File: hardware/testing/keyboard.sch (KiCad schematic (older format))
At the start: 1 part

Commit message: starting the testing PCB
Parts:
- removed U_Main1: proton_c, proton_c:proton_c, symbol proton_c:proton_c
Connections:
- no-connect marks 37 -> 0
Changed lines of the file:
@@
 $Descr A4 11693 8268
 encoding utf-8
-Sheet 1 2
+Sheet 1 5
 Title ""
 Date ""
@@
 $EndDescr
 $Sheet
-S 1650 2250 1900 1550
+S 3750 2750 700  1950
 U 5E25E984
 F0 "switch" 50
 F1 "switch.sch" 50
-F2 "ROW1" I R 3550 2300 50
-F3 "ROW2" I R 3550 2400 50
-F4 "ROW3" I R 3550 2500 50
-F5 "ROW4" I R 3550 2600 50
-F6 "COL1" I L 1650 2300 50
-F7 "COL2" I L 1650 2400 50
-F8 "COL3" I L 1650 2500 50
-F9 "COL4" I L 1650 2600 50
+F2 "ROW1" I R 4450 4600 50
+F3 "ROW2" I R 4450 4500 50
+F4 "ROW3" I R 4450 4400 50
+F5 "ROW4" I R 4450 4300 50
+F6 "ROW5" I R 4450 4200 50
+F7 "COL1" I R 4450 2800 50
+F8 "COL2" I R 4450 2900 50
+F9 "COL3" I R 4450 3000 50
+F10 "COL4" I R 4450 3100 50
+F11 "COL5" I R 4450 3200 50
+F12 "COL6" I R 4450 3300 50
+F13 "COL7" I R 4450 3400 50
+F14 "COL8" I R 4450 3500 50
+F15 "COL9" I R 4450 3600 50
+F16 "COL10" I R 4450 3700 50
+F17 "COL11" I R 4450 3800 50
+F18 "COL12" I R 4450 3900 50
+F19 "COL13" I R 4450 4000 50
+F20 "COL14" I R 4450 4100 50
+$EndSheet
+$Sheet
+S 5500 2450 800  2250
+U 5E1424B2
+F0 "SMT32" 50
+F1 "SMT32.sch" 50
+F2 "I2C2_SDA" I R 6300 2900 50
+F3 "I2C2_SCL" I R 6300 2800 50
+F4 "COL1" I L 5500 2800 50
+F5 "COL2" I L 5500 2900 50
+F6 "COL3" I L 5500 3000 50
+F7 "COL4" I L 5500 3100 50
+F8 "COL5" I L 5500 3200 50
+F9 "COL6" I L 5500 3300 50
+F10 "COL7" I L 5500 3400 50
+F11 "COL8" I L 5500 3500 50
+F12 "COL9" I L 5500 3600 50
+F13 "COL10" I L 5500 3700 50
+F14 "COL11" I L 5500 3800 50
+F15 "COL12" I L 5500 3900 50
+F16 "COL13" I L 5500 4000 50
+F17 "COL14" I L 5500 4100 50
+F18 "ROW5" I L 5500 4200 50
+F19 "ROW4" I L 5500 4300 50
+F20 "ROW3" I L 5500 4400 50
+F21 "ROW2" I L 5500 4500 50
+F22 "ROW1" I L 5500 4600 50
+F23 "LED_EN_PIN" I R 6300 3000 50
 $EndSheet
 Wire Wire Line
-	7050 2350 3600 2350
+	5500 2800 4450 2800
 Wire Wire Line
-	3600 2350 3600 2400
+	4450 2900 5500 2900
 Wire Wire Line
-	3600 2400 3550 2400
+	5500 3000 4450 3000
 Wire Wire Line
-	7050 2450 3600 2450
+	4450 3100 5500 3100
 Wire Wire Line
-	3600 2450 3600 2500
+	5500 3200 4450 3200
 Wire Wire Line
-	3600 2500 3550 2500
+	4450 3300 5500 3300
 Wire Wire Line
-	3550 2600 3600 2600
+	5500 3400 4450 3400
 Wire Wire Line
-	3600 2600 3600 2550
+	4450 3500 5500 3500
 Wire Wire Line
-	3600 2550 7050 2550
+	5500 3600 4450 3600
 Wire Wire Line
-	7050 2050 3600 2050
+	4450 3700 5500 3700
 Wire Wire Line
-	3600 2050 3600 2300
+	5500 3800 4450 3800
 Wire Wire Line
-	3600 2300 3550 2300
+	4450 3900 5500 3900
 Wire Wire Line
-	1650 2300 1550 2300
+	5500 4000 4450 4000
 Wire Wire Line
-	1550 2300 1550 1500
+	4450 4100 5500 4100
 Wire Wire Line
-	1550 1500 9200 1500
+	5500 4200 4450 4200
 Wire Wire Line
-	9200 1500 9200 2350
+	4450 4300 5500 4300
 Wire Wire Line
-	9200 2350 9100 2350
+	5500 4400 4450 4400
 Wire Wire Line
-	9100 2450 9250 2450
+	4450 4500 5500 4500
 Wire Wire Line
-	9250 2450 9250 1400
+	5500 4600 4450 4600
 Wire Wire Line
-	9250 1400 1500 1400
+	6300 3000 6700 3000
 Wire Wire Line
-	1500 1400 1500 2400
+	6700 2900 6300 2900
 Wire Wire Line
-	1500 2400 1650 2400
-Wire Wire Line
-	1650 2500 1450 2500
-Wire Wire Line
-	1450 2500 1450 1300
-Wire Wire Line
-	9300 1300 9300 2550
-Wire Wire Line
-	9300 2550 9100 2550
-Wire Wire Line
-	1400 1250 9350 1250
-Wire Wire Line
-	9350 1250 9350 2650
-Wire Wire Line
-	9350 2650 9100 2650
-Wire Wire Line
-	1450 1300 9300 1300
-$Comp
-L proton_c:proton_c U_Main1
-U 1 1 5E06F676
-P 8100 2950
-F 0 "U_Main1" H 8075 1427 50  0000 C CNN
-F 1 "proton_c" H 8075 1336 50  0000 C CNN
-F 2 "proton_c:proton_c" H 7950 2950 50  0001 C CNN
-F 3 "" H 7950 2950 50  0001 C CNN
-	1    8100 2950
-	1    0    0    -1
-$EndComp
-Wire Wire Line
-	1400 1250 1400 2600
-Wire Wire Line
-	1400 2600 1650 2600
-NoConn ~ 9100 1950
-NoConn ~ 9100 2050
-NoConn ~ 9100 2150
-NoConn ~ 9100 2250
-NoConn ~ 9100 2750
-NoConn ~ 9100 2850
-NoConn ~ 9100 2950
-NoConn ~ 8250 1650
-NoConn ~ 7900 1650
-NoConn ~ 7800 1650
-NoConn ~ 7700 1650
-NoConn ~ 7050 1950
-NoConn ~ 7050 2150
-NoConn ~ 7050 2250
-NoConn ~ 7050 2650
-NoConn ~ 7050 2750
-NoConn ~ 7050 2850
-NoConn ~ 7050 2950
-NoConn ~ 7050 3050
-NoConn ~ 7050 3400
-NoConn ~ 7050 3850
-NoConn ~ 7050 3950
-NoConn ~ 7050 4050
-NoConn ~ 7050 4150
-NoConn ~ 7050 4250
-NoConn ~ 7050 4350
-NoConn ~ 9100 4350
-NoConn ~ 9100 4250
-NoConn ~ 9100 4150
-NoConn ~ 9100 4050
-NoConn ~ 9100 3950
-NoConn ~ 9100 3850
-NoConn ~ 9100 3550
-NoConn ~ 9100 3450
-NoConn ~ 9100 3350
-NoConn ~ 9100 3250
-NoConn ~ 9100 3050
+	6300 2800 6700 2800
+$Sheet
+S 6700 2750 600  350
+U 5EC33E3D
+F0 "RGB" 50
+F1 "RGB.sch" 50
+F2 "SCL" I L 6700 2800 50
+F3 "SDA" I L 6700 2900 50
+F4 "LED_EN_PIN" I L 6700 3000 50
+$EndSheet
 $EndSCHEMATC

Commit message: remove useless files
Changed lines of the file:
@@
 $Descr A4 11693 8268
 encoding utf-8
-Sheet 1 5
+Sheet 1 3
 Title ""
 Date ""
@@
 Wire Wire Line
 	5500 4600 4450 4600
-Wire Wire Line
-	6300 3000 6700 3000
-Wire Wire Line
-	6700 2900 6300 2900
-Wire Wire Line
-	6300 2800 6700 2800
-$Sheet
-S 6700 2750 600  350
-U 5EC33E3D
-F0 "RGB" 50
-F1 "RGB.sch" 50
-F2 "SCL" I L 6700 2800 50
-F3 "SDA" I L 6700 2900 50
-F4 "LED_EN_PIN" I L 6700 3000 50
-$EndSheet
 $EndSCHEMATC

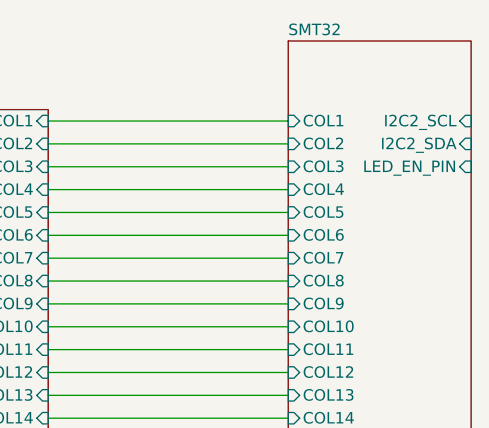
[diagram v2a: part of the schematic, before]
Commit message: making testing PCB, making sure the DFU mode is correct
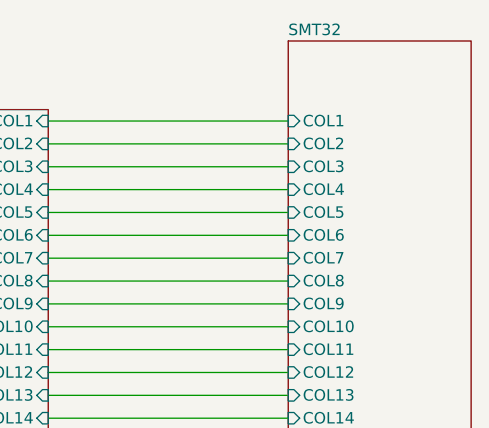
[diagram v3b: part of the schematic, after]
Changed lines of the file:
@@
 F0 "SMT32" 50
 F1 "SMT32.sch" 50
-F2 "I2C2_SDA" I R 6300 2900 50
-F3 "I2C2_SCL" I R 6300 2800 50
-F4 "COL1" I L 5500 2800 50
-F5 "COL2" I L 5500 2900 50
-F6 "COL3" I L 5500 3000 50
-F7 "COL4" I L 5500 3100 50
-F8 "COL5" I L 5500 3200 50
-F9 "COL6" I L 5500 3300 50
-F10 "COL7" I L 5500 3400 50
-F11 "COL8" I L 5500 3500 50
-F12 "COL9" I L 5500 3600 50
-F13 "COL10" I L 5500 3700 50
-F14 "COL11" I L 5500 3800 50
-F15 "COL12" I L 5500 3900 50
-F16 "COL13" I L 5500 4000 50
-F17 "COL14" I L 5500 4100 50
-F18 "ROW5" I L 5500 4200 50
-F19 "ROW4" I L 5500 4300 50
-F20 "ROW3" I L 5500 4400 50
-F21 "ROW2" I L 5500 4500 50
-F22 "ROW1" I L 5500 4600 50
-F23 "LED_EN_PIN" I R 6300 3000 50
+F2 "COL1" I L 5500 2800 50
+F3 "COL2" I L 5500 2900 50
+F4 "COL3" I L 5500 3000 50
+F5 "COL4" I L 5500 3100 50
+F6 "COL5" I L 5500 3200 50
+F7 "COL6" I L 5500 3300 50
+F8 "COL7" I L 5500 3400 50
+F9 "COL8" I L 5500 3500 50
+F10 "COL9" I L 5500 3600 50
+F11 "COL10" I L 5500 3700 50
+F12 "COL11" I L 5500 3800 50
+F13 "COL12" I L 5500 3900 50
+F14 "COL13" I L 5500 4000 50
+F15 "COL14" I L 5500 4100 50
+F16 "ROW5" I L 5500 4200 50
+F17 "ROW4" I L 5500 4300 50
+F18 "ROW3" I L 5500 4400 50
+F19 "ROW2" I L 5500 4500 50
+F20 "ROW1" I L 5500 4600 50
 $EndSheet
 Wire Wire Line
